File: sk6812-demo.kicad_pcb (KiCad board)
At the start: 2 copper layers, 76.2 x 50.8 mm, 9 parts, among them U1 Photon

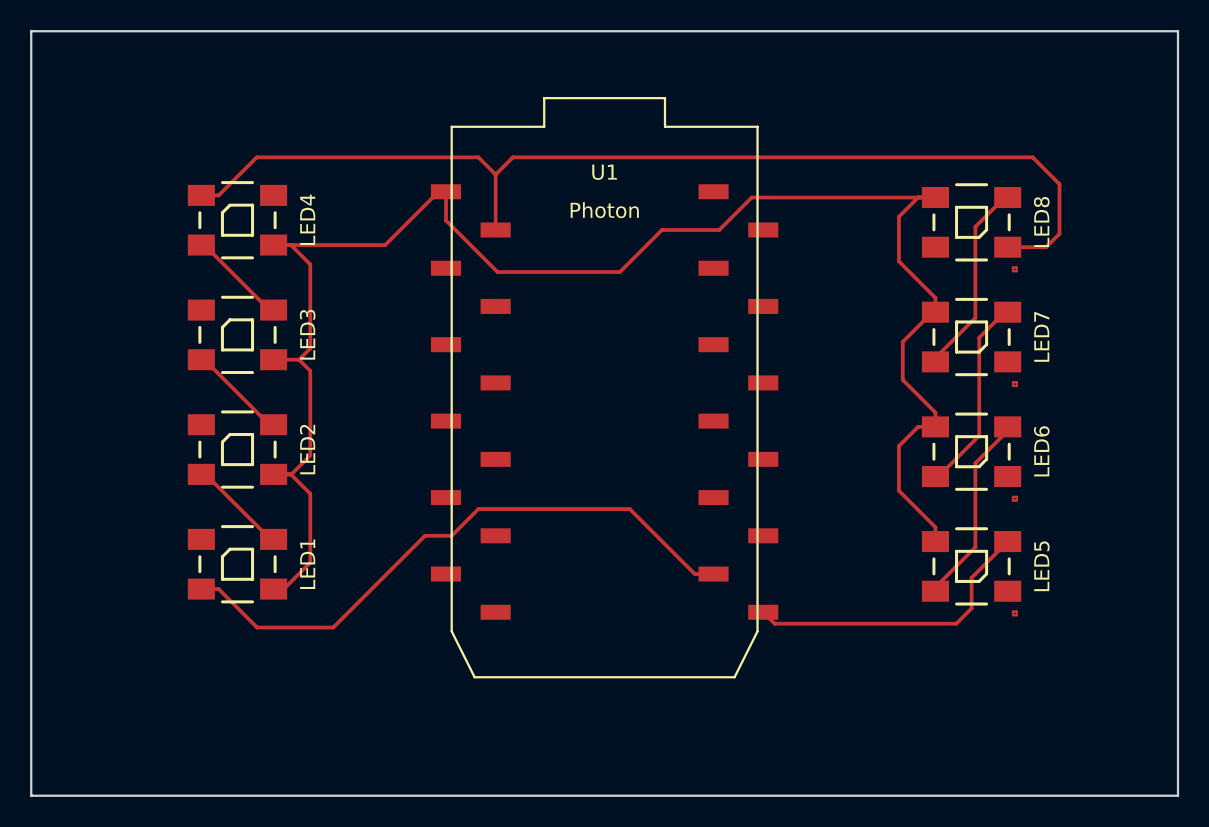
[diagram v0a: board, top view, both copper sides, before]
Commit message: Fixing power nets
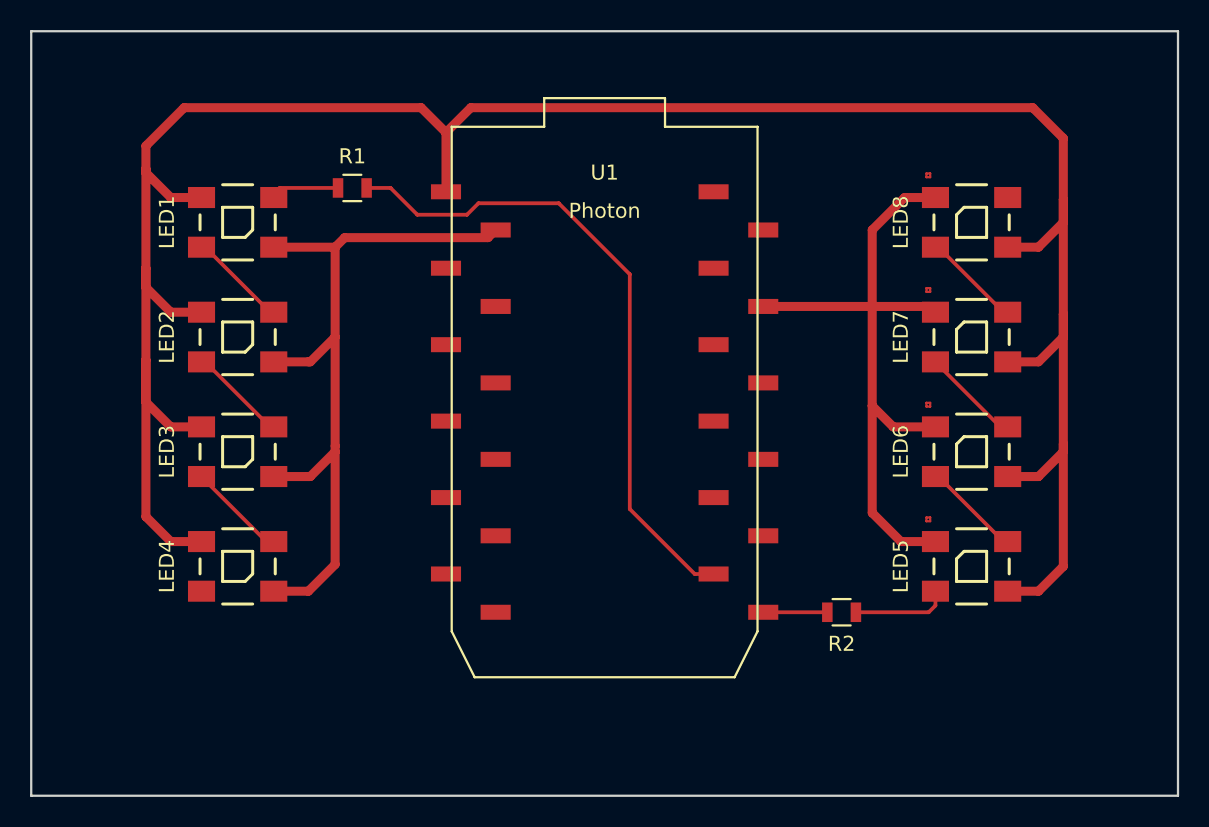
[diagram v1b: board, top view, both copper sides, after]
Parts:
- added R1: R, Resistors_SMD:R_0805, F.Cu at (122.9, 86.6)
- added R2: R, Resistors_SMD:R_0805, F.Cu at (155.4, 114.8)
- moved LED4 23.0 mm to (115.3, 111.8), turned to 90 degrees
- moved LED1 22.7 mm to (115.3, 88.9), turned to 90 degrees
- moved LED3 7.76 mm to (115.3, 104.1), turned to 90 degrees
- moved LED2 7.48 mm to (115.3, 96.5), turned to 90 degrees
- turned LED5 to 90 degrees
- turned LED6 to 90 degrees
- turned LED7 to 90 degrees
- turned LED8 to 90 degrees
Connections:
- U1 pad 13: Net-(LED5-Pad2) -> Net-(R2-Pad2)
- U1 pad 14: Net-(LED1-Pad4) -> Net-(R1-Pad2)
- U1 pad 21: (no net) -> GND
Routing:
- net +5V: track 112.6 -> 164.2 mm
- net Net-(R1-Pad2): track 0.00 -> 43.4 mm
- net Net-(LED1-Pad4): track 40.1 -> 4.68 mm
- net GND: track 70.5 -> 95.9 mm
- net Net-(LED5-Pad2): track 20.0 -> 6.42 mm
- net Net-(LED6-Pad4): track 13.1 -> 6.60 mm
- net Net-(LED7-Pad4): track 13.0 -> 6.59 mm
- net Net-(LED5-Pad4): track 12.9 -> 6.59 mm
- net Net-(R2-Pad2): track 0.00 -> 4.26 mm
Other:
- net class power added: clearance 0.2, trace_width 0.4, via_dia 0.6, via_drill 0.4
